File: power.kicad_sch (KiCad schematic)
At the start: 10 parts, among them J20 Screw_Terminal_01x02, U6 AMS1117-3.3 SOT-223

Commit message: symbols an footprints added for f411 change. ERC passes.
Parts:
- C15, C16, C5, C6, C7, C8: footprint ProjectLib:C_0402_1005Metric -> ProjectLib:C_0805_2012Metric
- D3: footprint ProjectLib:SOT-23 -> Package_TO_SOT_SMD:SOT-23
- U6: footprint ProjectLib:SOT-223 -> Package_TO_SOT_SMD:SOT-223-3_TabPin2
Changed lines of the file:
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@@
 			)
 		)
-		(property "Footprint" "ProjectLib:SOT-223"
+		(property "Footprint" "Package_TO_SOT_SMD:SOT-223-3_TabPin2"
 			(at 152.4 92.71 0)
 			(effects
@@
 			)
 		)
-		(property "Footprint" "ProjectLib:C_0402_1005Metric"
+		(property "Footprint" "ProjectLib:C_0805_2012Metric"
 			(at 110.7948 95.25 0)
 			(effects
@@
 			)
 		)
-		(property "Datasheet" ""
+		(property "Datasheet" "~"
 			(at 111.76 91.44 0)
 			(effects
@@
 			)
 		)
-		(property "Footprint" "ProjectLib:C_0402_1005Metric"
+		(property "Footprint" "ProjectLib:C_0805_2012Metric"
 			(at 101.9048 95.25 0)
 			(effects
@@
 			)
 		)
-		(property "Datasheet" ""
+		(property "Datasheet" "~"
 			(at 102.87 91.44 0)
 			(effects
@@
 			)
 		)
-		(property "Datasheet" "https://www.te.com/commerce/DocumentDelivery/DDEController?Action=srchrtrv&DocNm=BAT-HLD-012-SMT&DocType=Data+Sheet&DocLang=English&DocFormat=pdf&PartCntxt=BAT-HLD-012-SMT"
+		(property "Datasheet" "~"
 			(at 160.02 121.666 90)
 			(effects
@@
 			)
 		)
-		(property "Description" "12mm coin battery retainer smd"
+		(property "Description" "Single-cell battery"
 			(at 160.02 123.19 0)
 			(effects
@@
 			)
 		)
-		(property "Datasheet" "https://www.lcsc.com/datasheet/C474920.pdf"
+		(property "Datasheet" "~"
 			(at 152.4 68.58 0)
 			(effects
@@
 			)
 		)
-		(property "Description" "Screw terminal 1x02"
+		(property "Description" "Generic screw terminal, single row, 01x02, script generated (kicad-library-utils/schlib/autogen/connector/)"
 			(at 152.4 68.58 0)
 			(effects
@@
 			)
 		)
-		(property "Footprint" "ProjectLib:C_0402_1005Metric"
+		(property "Footprint" "ProjectLib:C_0805_2012Metric"
 			(at 84.1248 95.25 0)
 			(effects
@@
 			)
 		)
-		(property "Datasheet" ""
+		(property "Datasheet" "~"
 			(at 85.09 91.44 0)
 			(effects
@@
 			)
 		)
-		(property "Footprint" "ProjectLib:SOT-23"
+		(property "Footprint" "Package_TO_SOT_SMD:SOT-23"
 			(at 146.685 121.285 0)
 			(effects
@@
 			)
 		)
-		(property "Footprint" "ProjectLib:C_0402_1005Metric"
+		(property "Footprint" "ProjectLib:C_0805_2012Metric"
 			(at 157.1752 102.87 0)
 			(effects
@@
 			)
 		)
-		(property "Datasheet" ""
+		(property "Datasheet" "~"
 			(at 156.21 99.06 0)
 			(effects
@@
 			)
 		)
-		(property "Footprint" "ProjectLib:C_0402_1005Metric"
+		(property "Footprint" "ProjectLib:C_0805_2012Metric"
 			(at 120.3452 74.93 0)
 			(effects
@@
 			)
 		)
-		(property "Datasheet" ""
+		(property "Datasheet" "~"
 			(at 119.38 71.12 0)
 			(effects
@@
 		(dnp no)
 		(fields_autoplaced yes)
-		(property "Reference" "#PWR030"
+		(property "Reference" "#PWR0113"
 			(at 147.32 60.96 0)
 			(effects
@@
 			(project ""
 				(path "/0c2d0c14-8850-4a30-bb78-b2f40cb442ba/872e59d9-aae9-4a0c-a438-0cad18134c8d"
-					(reference "#PWR030")
+					(reference "#PWR0113")
 					(unit 1)
 				)
@@
 			)
 		)
-		(property "Footprint" "ProjectLib:C_0402_1005Metric"
+		(property "Footprint" "ProjectLib:C_0805_2012Metric"
 			(at 94.2848 95.25 0)
 			(effects
@@
 			)
 		)
-		(property "Datasheet" ""
+		(property "Datasheet" "~"
 			(at 95.25 91.44 0)
 			(effects

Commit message: ongoing
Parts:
- C15, C16, C5, C6, C7, C8: footprint ProjectLib:C_0805_2012Metric -> ProjectLib:C_0402_1005Metric
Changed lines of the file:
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@@
 			)
 		)
-		(property "Footprint" "ProjectLib:C_0805_2012Metric"
+		(property "Footprint" "ProjectLib:C_0402_1005Metric"
 			(at 110.7948 95.25 0)
 			(effects
@@
 			)
 		)
-		(property "Footprint" "ProjectLib:C_0805_2012Metric"
+		(property "Footprint" "ProjectLib:C_0402_1005Metric"
 			(at 101.9048 95.25 0)
 			(effects
@@
 			)
 		)
-		(property "Footprint" "ProjectLib:C_0805_2012Metric"
+		(property "Footprint" "ProjectLib:C_0402_1005Metric"
 			(at 84.1248 95.25 0)
 			(effects
@@
 			)
 		)
-		(property "Footprint" "ProjectLib:C_0805_2012Metric"
+		(property "Footprint" "ProjectLib:C_0402_1005Metric"
 			(at 157.1752 102.87 0)
 			(effects
@@
 			)
 		)
-		(property "Footprint" "ProjectLib:C_0805_2012Metric"
+		(property "Footprint" "ProjectLib:C_0402_1005Metric"
 			(at 120.3452 74.93 0)
 			(effects
@@
 			)
 		)
-		(property "Footprint" "ProjectLib:C_0805_2012Metric"
+		(property "Footprint" "ProjectLib:C_0402_1005Metric"
 			(at 94.2848 95.25 0)
 			(effects

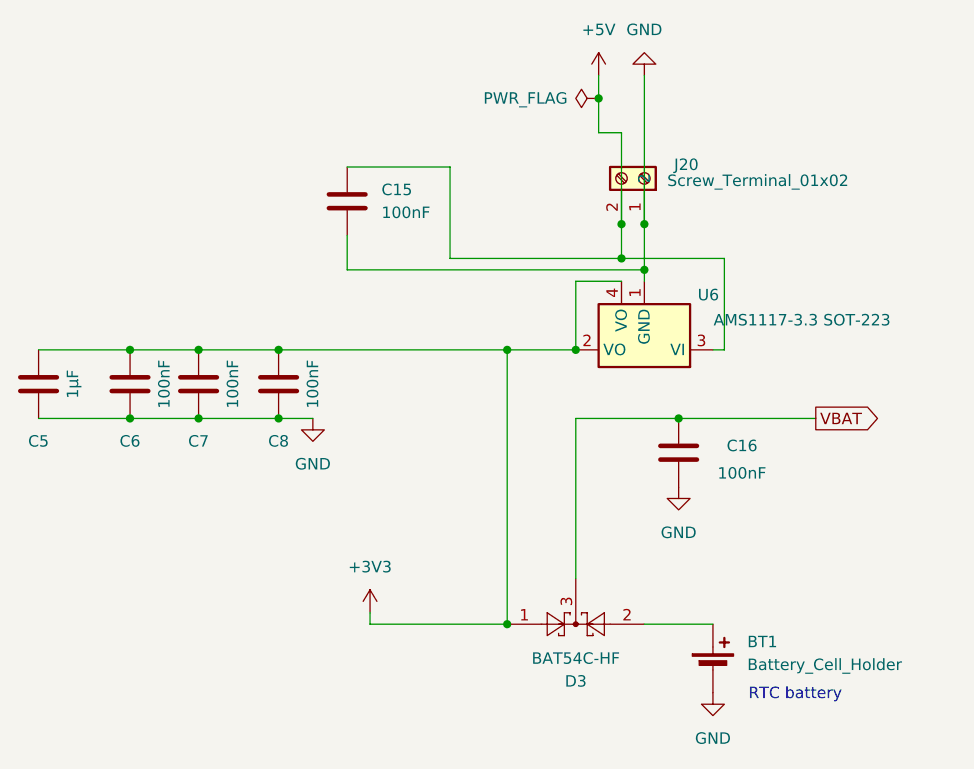
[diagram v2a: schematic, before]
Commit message: adding MCU, ongoing.
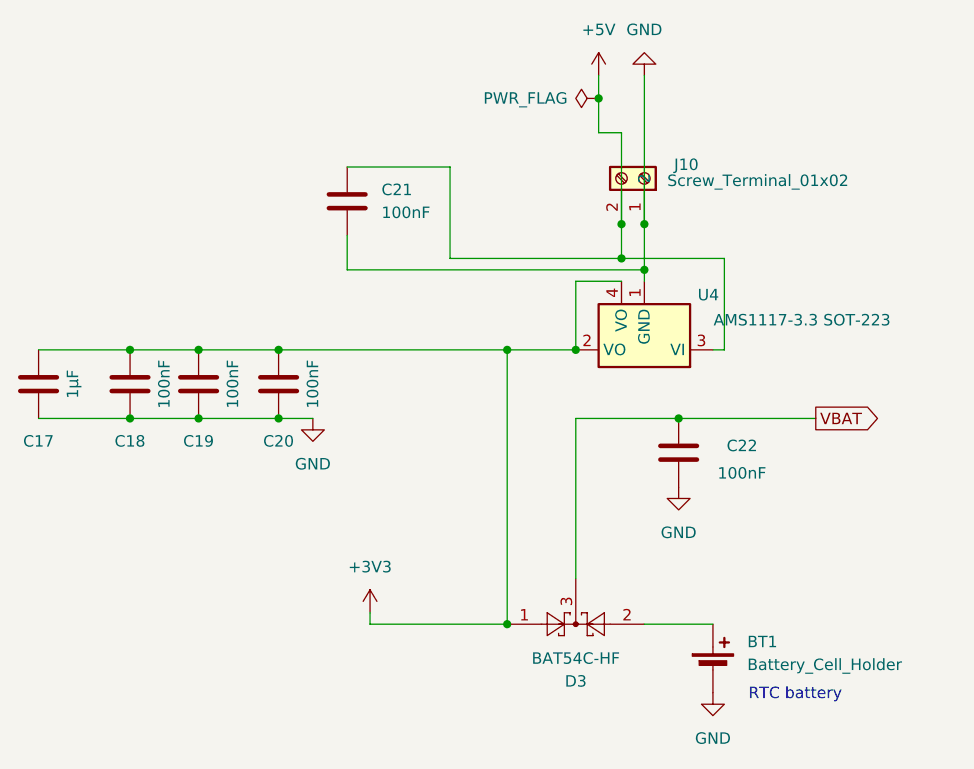
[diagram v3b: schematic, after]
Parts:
- renumbered C5 to C17, C6 to C18, C7 to C19, C8 to C20, C15 to C21, C16 to C22, J20 to J10, U6 to U4
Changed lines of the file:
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@@
 		(dnp no)
 		(fields_autoplaced yes)
-		(property "Reference" "#PWR042"
+		(property "Reference" "#PWR072"
 			(at 121.92 120.65 0)
 			(effects
@@
 			(project "SensorProject_t16-pcb"
 				(path "/0c2d0c14-8850-4a30-bb78-b2f40cb442ba/872e59d9-aae9-4a0c-a438-0cad18134c8d"
-					(reference "#PWR042")
+					(reference "#PWR072")
 					(unit 1)
 				)
@@
 		(on_board yes)
 		(dnp no)
-		(property "Reference" "U6"
+		(property "Reference" "U4"
 			(at 159.512 81.534 0)
 			(effects
@@
 			(project "SensorProject_t16-pcb"
 				(path "/0c2d0c14-8850-4a30-bb78-b2f40cb442ba/872e59d9-aae9-4a0c-a438-0cad18134c8d"
-					(reference "U6")
+					(reference "U4")
 					(unit 1)
 				)
@@
 		(on_board yes)
 		(dnp no)
-		(property "Reference" "#FLG03"
+		(property "Reference" "#FLG01"
 			(at 145.415 59.69 0)
 			(effects
@@
 			(project ""
 				(path "/0c2d0c14-8850-4a30-bb78-b2f40cb442ba/872e59d9-aae9-4a0c-a438-0cad18134c8d"
-					(reference "#FLG03")
+					(reference "#FLG01")
 					(unit 1)
 				)
@@
 		(dnp no)
 		(fields_autoplaced yes)
-		(property "Reference" "#PWR041"
+		(property "Reference" "#PWR074"
 			(at 152.4 50.8 0)
 			(effects
@@
 			(project "SensorProject_t16-pcb"
 				(path "/0c2d0c14-8850-4a30-bb78-b2f40cb442ba/872e59d9-aae9-4a0c-a438-0cad18134c8d"
-					(reference "#PWR041")
+					(reference "#PWR074")
 					(unit 1)
 				)
@@
 		(on_board yes)
 		(dnp no)
-		(property "Reference" "C8"
+		(property "Reference" "C20"
 			(at 111.76 97.79 0)
 			(effects
@@
 			(project "SensorProject_t16-pcb"
 				(path "/0c2d0c14-8850-4a30-bb78-b2f40cb442ba/872e59d9-aae9-4a0c-a438-0cad18134c8d"
-					(reference "C8")
+					(reference "C20")
 					(unit 1)
 				)
@@
 		(on_board yes)
 		(dnp no)
-		(property "Reference" "C7"
+		(property "Reference" "C19"
 			(at 102.87 97.79 0)
 			(effects
@@
 			(project "SensorProject_t16-pcb"
 				(path "/0c2d0c14-8850-4a30-bb78-b2f40cb442ba/872e59d9-aae9-4a0c-a438-0cad18134c8d"
-					(reference "C7")
+					(reference "C19")
 					(unit 1)
 				)
@@
 		(on_board yes)
 		(dnp no)
-		(property "Reference" "J20"
+		(property "Reference" "J10"
 			(at 155.702 67.056 90)
 			(effects
@@
 			(project "SensorProject_t16-pcb"
 				(path "/0c2d0c14-8850-4a30-bb78-b2f40cb442ba/872e59d9-aae9-4a0c-a438-0cad18134c8d"
-					(reference "J20")
+					(reference "J10")
 					(unit 1)
 				)
@@
 		(dnp no)
 		(fields_autoplaced yes)
-		(property "Reference" "#PWR050"
+		(property "Reference" "#PWR071"
 			(at 115.57 101.6 0)
 			(effects
@@
 			(project "SensorProject_t16-pcb"
 				(path "/0c2d0c14-8850-4a30-bb78-b2f40cb442ba/872e59d9-aae9-4a0c-a438-0cad18134c8d"
-					(reference "#PWR050")
+					(reference "#PWR071")
 					(unit 1)
 				)
@@
 		(on_board yes)
 		(dnp no)
-		(property "Reference" "C5"
+		(property "Reference" "C17"
 			(at 85.09 97.79 0)
 			(effects
@@
 			(project "SensorProject_t16-pcb"
 				(path "/0c2d0c14-8850-4a30-bb78-b2f40cb442ba/872e59d9-aae9-4a0c-a438-0cad18134c8d"
-					(reference "C5")
+					(reference "C17")
 					(unit 1)
 				)
@@
 		(on_board yes)
 		(dnp no)
-		(property "Reference" "C16"
+		(property "Reference" "C22"
 			(at 161.544 98.298 0)
 			(effects
@@
 			(project ""
 				(path "/0c2d0c14-8850-4a30-bb78-b2f40cb442ba/872e59d9-aae9-4a0c-a438-0cad18134c8d"
-					(reference "C16")
+					(reference "C22")
 					(unit 1)
 				)
@@
 		(dnp no)
 		(fields_autoplaced yes)
-		(property "Reference" "C15"
+		(property "Reference" "C21"
 			(at 123.19 69.8499 0)
 			(effects
@@
 			(project ""
 				(path "/0c2d0c14-8850-4a30-bb78-b2f40cb442ba/872e59d9-aae9-4a0c-a438-0cad18134c8d"
-					(reference "C15")
+					(reference "C21")
 					(unit 1)
 				)
@@
 		(dnp no)
 		(fields_autoplaced yes)
-		(property "Reference" "#PWR078"
+		(property "Reference" "#PWR076"
 			(at 160.02 132.08 0)
 			(effects
@@
 			(project ""
 				(path "/0c2d0c14-8850-4a30-bb78-b2f40cb442ba/872e59d9-aae9-4a0c-a438-0cad18134c8d"
-					(reference "#PWR078")
+					(reference "#PWR076")
 					(unit 1)
 				)
@@
 		(dnp no)
 		(fields_autoplaced yes)
-		(property "Reference" "#PWR0113"
+		(property "Reference" "#PWR073"
 			(at 147.32 60.96 0)
 			(effects
@@
 			(project ""
 				(path "/0c2d0c14-8850-4a30-bb78-b2f40cb442ba/872e59d9-aae9-4a0c-a438-0cad18134c8d"
-					(reference "#PWR0113")
+					(reference "#PWR073")
 					(unit 1)
 				)
@@
 		(on_board yes)
 		(dnp no)
-		(property "Reference" "C6"
+		(property "Reference" "C18"
 			(at 95.25 97.79 0)
 			(effects
@@
 			(project "SensorProject_t16-pcb"
 				(path "/0c2d0c14-8850-4a30-bb78-b2f40cb442ba/872e59d9-aae9-4a0c-a438-0cad18134c8d"
-					(reference "C6")
+					(reference "C18")
 					(unit 1)
 				)

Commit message: th8-f411 with castellated MCU-LoRa. DRC clean, ERC with some warnings.
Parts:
- D3: footprint Package_TO_SOT_SMD:SOT-23 -> ProjectLib:SOT-23
- U4: footprint Package_TO_SOT_SMD:SOT-223-3_TabPin2 -> ProjectLib:SOT-223
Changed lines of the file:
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@@
 			)
 		)
-		(property "Footprint" "Package_TO_SOT_SMD:SOT-223-3_TabPin2"
+		(property "Footprint" "ProjectLib:SOT-223"
 			(at 152.4 92.71 0)
 			(effects
@@
 			)
 		)
-		(property "Footprint" "Package_TO_SOT_SMD:SOT-23"
+		(property "Footprint" "ProjectLib:SOT-23"
 			(at 146.685 121.285 0)
 			(effects

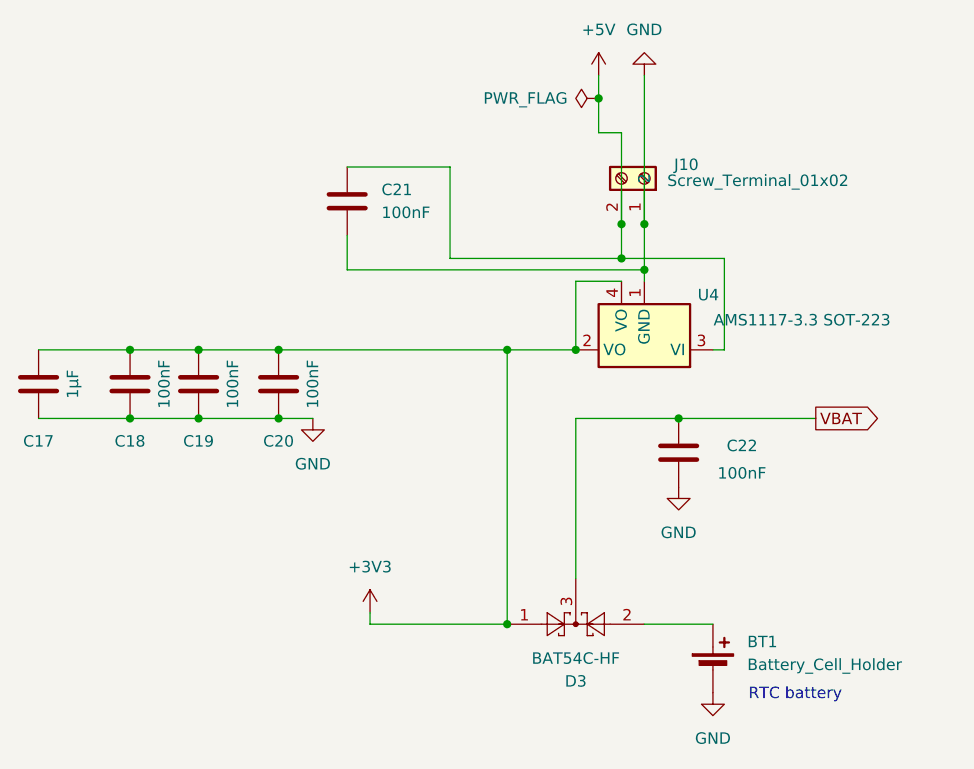
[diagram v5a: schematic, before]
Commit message: changed single 10k pull-up to 4.7k like others. Renumbered components to fill numbering gaps.
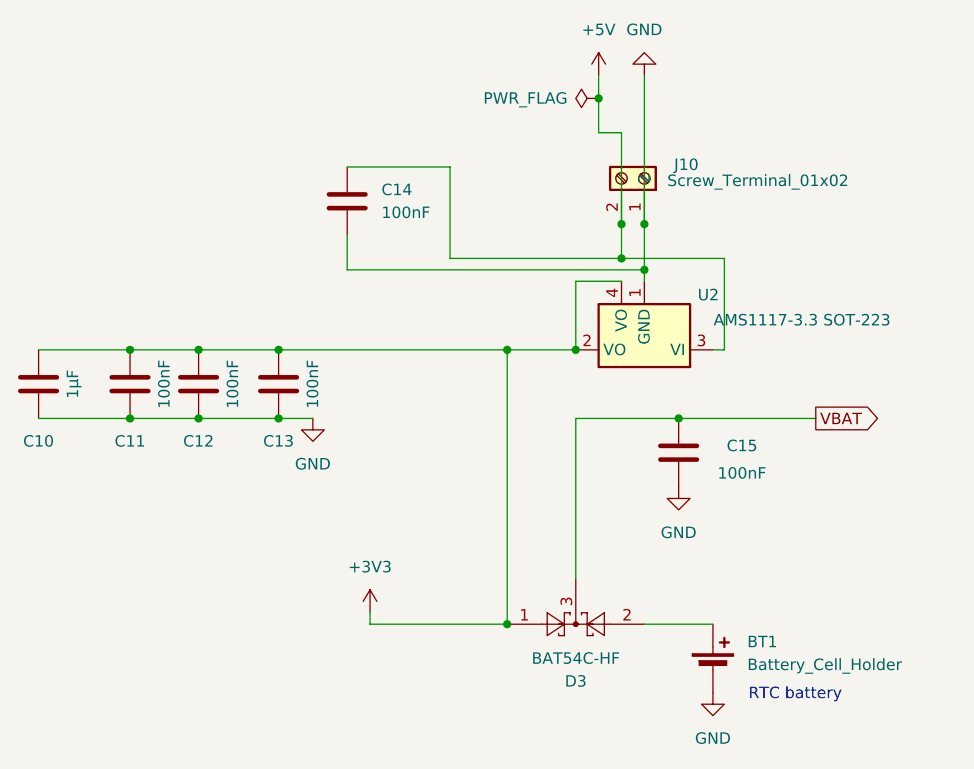
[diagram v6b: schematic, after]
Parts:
- renumbered C17 to C10, C18 to C11, C19 to C12, C20 to C13, C21 to C14, C22 to C15, U4 to U2
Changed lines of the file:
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@@
 		(on_board yes)
 		(dnp no)
-		(property "Reference" "U4"
+		(property "Reference" "U2"
 			(at 159.512 81.534 0)
 			(effects
@@
 			(project "SensorProject_t16-pcb"
 				(path "/0c2d0c14-8850-4a30-bb78-b2f40cb442ba/872e59d9-aae9-4a0c-a438-0cad18134c8d"
-					(reference "U4")
+					(reference "U2")
 					(unit 1)
 				)
@@
 		(on_board yes)
 		(dnp no)
-		(property "Reference" "C20"
+		(property "Reference" "C13"
 			(at 111.76 97.79 0)
 			(effects
@@
 			(project "SensorProject_t16-pcb"
 				(path "/0c2d0c14-8850-4a30-bb78-b2f40cb442ba/872e59d9-aae9-4a0c-a438-0cad18134c8d"
-					(reference "C20")
+					(reference "C13")
 					(unit 1)
 				)
@@
 		(on_board yes)
 		(dnp no)
-		(property "Reference" "C19"
+		(property "Reference" "C12"
 			(at 102.87 97.79 0)
 			(effects
@@
 			(project "SensorProject_t16-pcb"
 				(path "/0c2d0c14-8850-4a30-bb78-b2f40cb442ba/872e59d9-aae9-4a0c-a438-0cad18134c8d"
-					(reference "C19")
+					(reference "C12")
 					(unit 1)
 				)
@@
 		(on_board yes)
 		(dnp no)
-		(property "Reference" "C17"
+		(property "Reference" "C10"
 			(at 85.09 97.79 0)
 			(effects
@@
 			(project "SensorProject_t16-pcb"
 				(path "/0c2d0c14-8850-4a30-bb78-b2f40cb442ba/872e59d9-aae9-4a0c-a438-0cad18134c8d"
-					(reference "C17")
+					(reference "C10")
 					(unit 1)
 				)
@@
 		(on_board yes)
 		(dnp no)
-		(property "Reference" "C22"
+		(property "Reference" "C15"
 			(at 161.544 98.298 0)
 			(effects
@@
 			(project ""
 				(path "/0c2d0c14-8850-4a30-bb78-b2f40cb442ba/872e59d9-aae9-4a0c-a438-0cad18134c8d"
-					(reference "C22")
+					(reference "C15")
 					(unit 1)
 				)
@@
 		(dnp no)
 		(fields_autoplaced yes)
-		(property "Reference" "C21"
+		(property "Reference" "C14"
 			(at 123.19 69.8499 0)
 			(effects
@@
 			(project ""
 				(path "/0c2d0c14-8850-4a30-bb78-b2f40cb442ba/872e59d9-aae9-4a0c-a438-0cad18134c8d"
-					(reference "C21")
+					(reference "C14")
 					(unit 1)
 				)
@@
 		(on_board yes)
 		(dnp no)
-		(property "Reference" "C18"
+		(property "Reference" "C11"
 			(at 95.25 97.79 0)
 			(effects
@@
 			(project "SensorProject_t16-pcb"
 				(path "/0c2d0c14-8850-4a30-bb78-b2f40cb442ba/872e59d9-aae9-4a0c-a438-0cad18134c8d"
-					(reference "C18")
+					(reference "C11")
 					(unit 1)
 				)

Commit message: ongoing.
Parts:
- renumbered C13 to C?, C12 to C?, C10 to C?, C15 to C?, C14 to C?, C11 to C?, D3 to D?, J10 to J?, U2 to U?
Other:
- title: Multiplex I2C to Screw Terminal connectors -> Power Regulator & RTC Battery
